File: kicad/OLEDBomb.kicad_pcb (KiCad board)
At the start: 2 copper layers, 63.5 x 63.5 mm, 15 parts, among them J1 Button, J2 Button_LED, J3 Battery, Q1 Q_NPN_ECB, Q2 Q_NPN_CBE, Q3 Q_NPN_ECB, U1 TP4056Board, U2 OLED1.3SPI, U3 StepUp5V, U4 ARDUINO_PRO_MINI, U5 ADP7142AUJZ-3.3

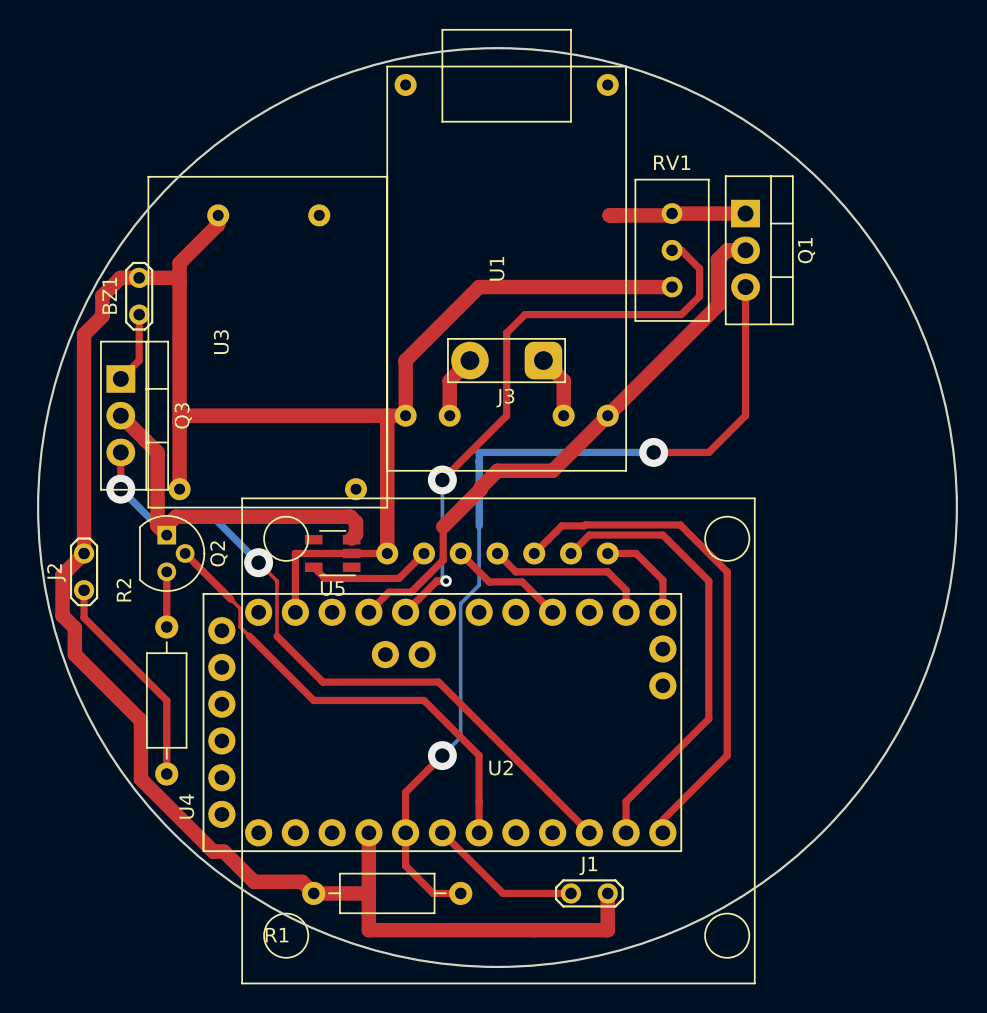
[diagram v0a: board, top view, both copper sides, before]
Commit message: Added English syllables Added ability to remove syllable limitations (no ellipses and the beginning and/or end of syllables) Added settings (hold the button): rus/eng syllables for bomb, small/big team for bomb, timer value, whether to use syllable limitations Added vibromotor support Added another PCB layout
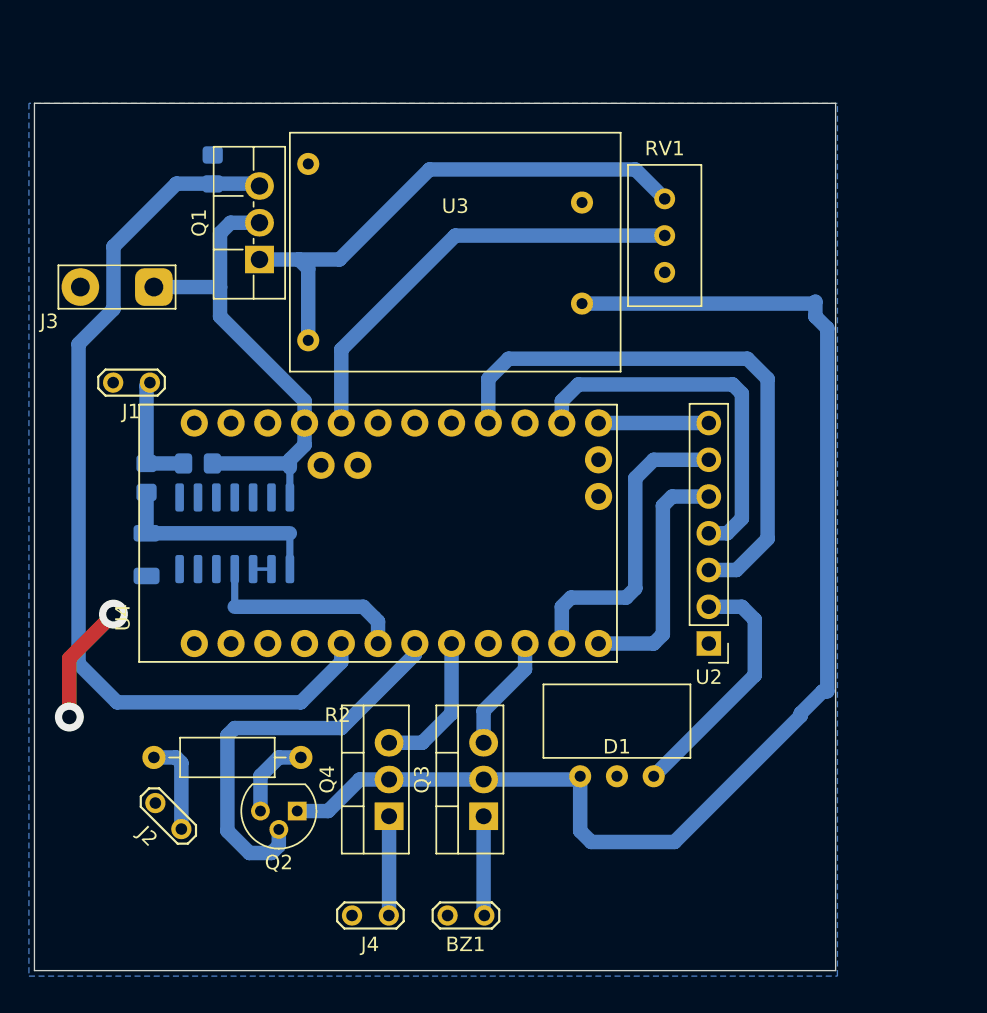
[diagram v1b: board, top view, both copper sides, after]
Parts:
- removed U5: ADP7142AUJZ-3.3, Package_TO_SOT_SMD:TSOT-23-5
- added C1: 10n, Capacitor_SMD:C_1206_3216Metric, B.Cu at (25.9, 49.0)
- added D1: StepDown3V3, MY:StepDown3V3, F.Cu at (61.0, 61.8)
- added J4: Vib, TestPoint:TestPoint_2Pads_Pitch2.54mm_Drill0.8mm, F.Cu at (42.7, 73.9)
- added Q4: Q_NPN_ECB, Package_TO_SOT_THT:TO-220-3_Vertical, F.Cu at (42.7, 67.1)
- added R3: 10k, Resistor_SMD:R_0805_2012Metric_Pad1.20x1.40mm_HandSolder, B.Cu at (29.5, 42.7)
- added R4: 10k, Resistor_SMD:R_0805_2012Metric_Pad1.20x1.40mm_HandSolder, B.Cu at (25.9, 43.7)
- Q1: footprint Package_TO_SOT_THT:TO-220-3_Vertical -> Package_TO_SOT_THT:TO-220F-3_Vertical
- R1: footprint Resistor_THT:R_Axial_DIN0207_L6.3mm_D2.5mm_P10.16mm_Horizontal -> Resistor_SMD:R_0805_2012Metric_Pad1.20x1.40mm_HandSolder; moved to B.Cu
- U1: value TP4056Board -> 74HC14; footprint ARDUINO_PRO_MINI:TP4056Board -> Package_SO:SOIC-14_3.9x8.7mm_P1.27mm; moved to B.Cu
- U2: footprint MY:Oled1.3SPI -> Connector_PinHeader_2.54mm:PinHeader_1x07_P2.54mm_Vertical
- U4: footprint ARDUINO_PRO_MINI:MODULE_ARDUINO_PRO_MINI -> MY:MODULE_ARDUINO_PRO_MINI_NO_PROG_PING
- moved R1 52.9 mm to (30.5, 22.4), turned to 90 degrees
- moved BZ1 47.9 mm to (49.3, 73.9), turned to 180 degrees
- moved J1 45.8 mm to (26.1, 37.1), turned to 180 degrees
- moved Q3 39.3 mm to (49.2, 67.1), turned to 90 degrees
- moved Q1 33.7 mm to (33.7, 28.6), turned to 90 degrees
- moved J3 27.4 mm to (26.4, 30.5)
- moved U1 24.3 mm to (32.0, 47.5), turned to 90 degrees
- moved Q2 21.1 mm to (36.3, 66.7), turned to 180 degrees
- moved J2 17.8 mm to (28.3, 67.9), turned to 135 degrees
- moved U2 16.0 mm to (64.8, 55.1), turned to 180 degrees
- moved U3 15.2 mm to (47.2, 27.4), turned to 180 degrees
- moved U4 13.8 mm to (41.9, 47.5)
- moved R2 1.45 mm to (26.4, 63.0), turned to 0 degrees
- moved RV1 1.14 mm to (61.7, 24.4)
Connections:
- J1 pad 1: Net-(J1-Pad1) -> Net-(J1-Pin_1)
- J3 pad 1: Net-(J3-Pad1) -> Net-(J3-Pin_1)
- J3 pad 2: Net-(J3-Pad2) -> GND
- Q1 pad 2: Net-(Q1-Pad2) -> Net-(J3-Pin_1)
- U1 pad 3: Net-(Q1-Pad2) -> Net-(U1-Pad2)
- U1 pad 4: Net-(J3-Pad1) -> Net-(U4-D3)
- U1 pad 5: Net-(J3-Pad2) -> (no net)
- U1 pad 6: GND -> (no net)
- U4 pad JP2_1: Net-(U4-PadJP2_1) -> unconnected-(U4-A4-PadJP2_1)
- U4 pad JP2_2: Net-(U4-PadJP2_2) -> unconnected-(U4-A5-PadJP2_2)
- U4 pad JP3_1: Net-(U4-PadJP3_1) -> unconnected-(U4-A6-PadJP3_1)
- U4 pad JP3_2: Net-(U4-PadJP3_2) -> unconnected-(U4-A7-PadJP3_2)
- U4 pad JP6_1: Net-(U4-PadJP6_1) -> unconnected-(U4-RAW-PadJP6_1)
- U4 pad JP6_10: Net-(U4-PadJP6_10) -> unconnected-(U4-MISO-PadJP6_10)
- U4 pad JP6_3: Net-(U4-PadJP6_3) -> unconnected-(U4-RST_1-PadJP6_3)
- U4 pad JP6_4: Net-(Q1-Pad2) -> Net-(J3-Pin_1)
- U4 pad JP6_6: Net-(U4-PadJP6_6) -> unconnected-(U4-A2-PadJP6_6)
- U4 pad JP6_7: Net-(U4-PadJP6_7) -> unconnected-(U4-A1-PadJP6_7)
- U4 pad JP6_8: Net-(U4-PadJP6_8) -> unconnected-(U4-A0-PadJP6_8)
- U4 pad JP7_10: Net-(U4-PadJP7_10) -> unconnected-(U4-RST_2-PadJP7_10)
- U4 pad JP7_11: Net-(U4-PadJP7_11) -> unconnected-(U4-RXI_2-PadJP7_11)
- U4 pad JP7_12: Net-(U4-PadJP7_12) -> unconnected-(U4-TXO_2-PadJP7_12)
- U4 pad JP7_4: Net-(U4-PadJP7_4) -> unconnected-(U4-D6-PadJP7_4)
- U4 pad JP7_7: Net-(J1-Pad1) -> Net-(U4-D3)
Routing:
- net GND: track 167.6 -> 8.37 mm, vias 0 -> 2
- net Net-(D1-VI): track 25.0 -> 89.6 mm
- net Net-(Q1-Pad2): track 39.7 -> 0.00 mm
- net Net-(Q3-B): track 47.0 -> 8.04 mm, vias 2 -> 0
- net Net-(J3-Pin_1): track 0.00 -> 33.8 mm
- net Net-(U2-SCK): track 8.03 -> 39.5 mm
- net Net-(Q1-E): track 10.1 -> 37.0 mm
- net Net-(U2-RES): track 34.5 -> 17.0 mm
- net Net-(C1-Pad2): track 0.00 -> 15.2 mm
- net Net-(U2-SDA): track 11.5 -> 26.0 mm
- net Net-(U4-D3): track 0.00 -> 14.5 mm
- net Net-(U4-A3): track 41.5 -> 30.7 mm, vias 2 -> 0
- net Net-(J1-Pad1): track 10.6 -> 0.00 mm
- net Net-(Q4-B): track 0.00 -> 9.99 mm
- net Net-(U2-DC): track 30.2 -> 21.4 mm
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- added copper zone on B.Cu, net GND
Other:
- board size 63.5 x 63.5 mm -> 55.4 x 59.9 mm
- net class Default removed
